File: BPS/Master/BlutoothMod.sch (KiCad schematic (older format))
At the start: 12 parts, among them J12 Conn_01x02, Q5 BSB008NE2LX, U6 RN4870-V_RM118, U7 MCP100-315D

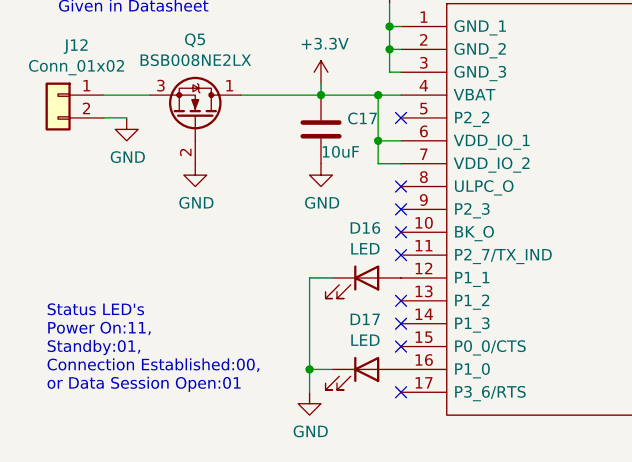
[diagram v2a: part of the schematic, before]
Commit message: Added UART_TX indicator light.
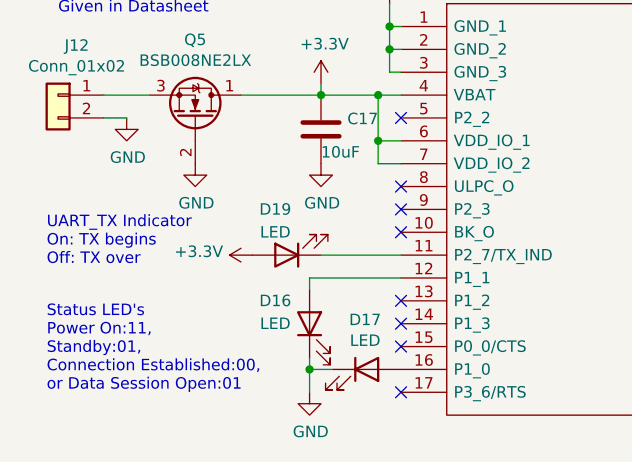
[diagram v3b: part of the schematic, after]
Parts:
- added D19: LED, symbol Device:LED
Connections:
- net +3V3: now also D19.2 (A)
- net at U6.11 (P2_7/TX_IND): now also D19.1 (K)
- no-connect marks 15 -> 14
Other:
- note added: "UART_TX Indicator\nOn: TX begins\nOff: TX over"
- moved on the sheet: D16
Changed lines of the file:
@@
 NoConn ~ 5000 4200
 NoConn ~ 5000 4100
-NoConn ~ 5000 3900
 NoConn ~ 5000 3800
 NoConn ~ 5000 3700
@@
 L Device:LED D16
 U 1 1 5EE20E59
-P 4850 4000
-F 0 "D16" H 4843 4217 50  0000 C CNN
-F 1 "LED" H 4843 4126 50  0000 C CNN
-F 2 "" H 4850 4000 50  0001 C CNN
-F 3 "~" H 4850 4000 50  0001 C CNN
-	1    4850 4000
-	1    0    0    -1
+P 4600 4200
+F 0 "D16" V 4700 4350 50  0000 C CNN
+F 1 "LED" V 4600 4350 50  0000 C CNN
+F 2 "" H 4600 4200 50  0001 C CNN
+F 3 "~" H 4600 4200 50  0001 C CNN
+	1    4600 4200
+	0    -1   -1   0
 $EndComp
 $Comp
@@
 $EndComp
 Wire Wire Line
-	4700 4000 4600 4000
-Wire Wire Line
-	4600 4000 4600 4400
-Wire Wire Line
 	4600 4400 4700 4400
 Wire Wire Line
 	4600 4400 4600 4500
-Connection ~ 4600 4400
 $Comp
 L power:GND #PWR0117
@@
 Text Notes 7450 3600 0    50   ~ 0
 RSSI Indicator\n(On: Strong)
+Wire Wire Line
+	4600 4400 4600 4350
+Connection ~ 4600 4400
+Wire Wire Line
+	4600 4050 4600 4000
+Wire Wire Line
+	4600 4000 5000 4000
+$Comp
+L Device:LED D19
+U 1 1 5EE52339
+P 4500 3900
+F 0 "D19" H 4550 3700 50  0000 C CNN
+F 1 "LED" H 4550 3800 50  0000 C CNN
+F 2 "" H 4500 3900 50  0001 C CNN
+F 3 "~" H 4500 3900 50  0001 C CNN
+	1    4500 3900
+	-1   0    0    1
+$EndComp
+$Comp
+L power:+3.3V #PWR028
+U 1 1 5EE5298C
+P 4350 3900
+F 0 "#PWR028" H 4350 3750 50  0001 C CNN
+F 1 "+3.3V" V 4365 4028 50  0000 L CNN
+F 2 "" H 4350 3900 50  0001 C CNN
+F 3 "" H 4350 3900 50  0001 C CNN
+	1    4350 3900
+	0    -1   -1   0
+$EndComp
+Wire Wire Line
+	4650 3900 5000 3900
+Text Notes 3450 3950 0    50   ~ 0
+UART_TX Indicator\nOn: TX begins\nOff: TX over
 $EndSCHEMATC

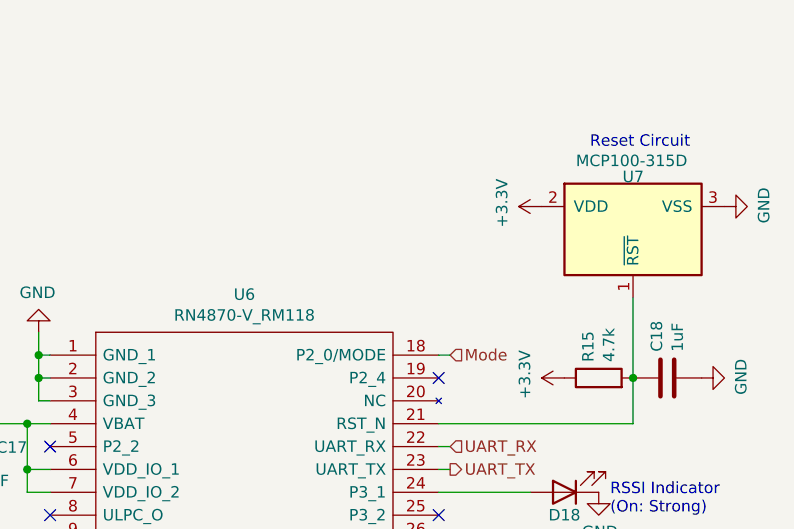
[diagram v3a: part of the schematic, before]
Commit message: The setup for bluetooth mode can't be done through a port using the STM so I used a switch instead, we can use that to toggle between Application mode and testing mode.
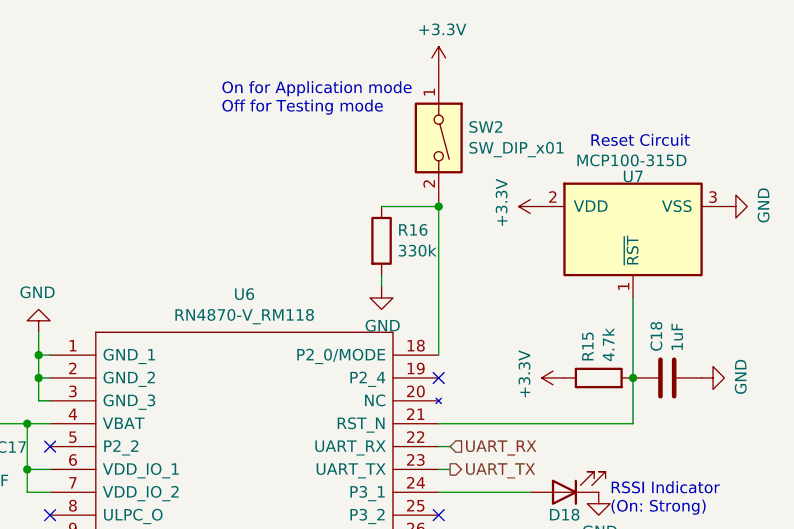
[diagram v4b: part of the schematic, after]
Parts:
- added R16: 330k, symbol Device:R
- added SW2: SW_DIP_x01, symbol Switch:SW_DIP_x01
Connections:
- net +3V3: now also SW2.1
- net GND: now also R16.2
- net Mode: no longer names the net of U6.18 (P2_0/MODE)
- net Mode: now also R16.1, SW2.2
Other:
- note added: "On for Application mode\nOff for Testing mode"
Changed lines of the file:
@@
 	1    0    0    -1
 $EndComp
-Text HLabel 6750 2900 2    50   Input ~ 0
-Mode
 Text Notes 3500 2850 0    50   ~ 0
 Reverse Voltage Protection Circuit\nGiven in Datasheet
@@
 Wire Wire Line
 	6700 3400 6750 3400
-Wire Wire Line
-	6700 2900 6750 2900
 $Comp
 L Power_Supervisor:MCP100-315D U7
@@
 Text Notes 3450 3950 0    50   ~ 0
 UART_TX Indicator\nOn: TX begins\nOff: TX over
+$Comp
+L Switch:SW_DIP_x01 SW2
+U 1 1 5EE36BE3
+P 6700 1950
+F 0 "SW2" V 6654 2080 50  0000 L CNN
+F 1 "SW_DIP_x01" V 6745 2080 50  0000 L CNN
+F 2 "" H 6700 1950 50  0001 C CNN
+F 3 "~" H 6700 1950 50  0001 C CNN
+	1    6700 1950
+	0    1    1    0
+$EndComp
+$Comp
+L power:+3.3V #PWR035
+U 1 1 5EE37A78
+P 6700 1650
+F 0 "#PWR035" H 6700 1500 50  0001 C CNN
+F 1 "+3.3V" H 6715 1823 50  0000 C CNN
+F 2 "" H 6700 1650 50  0001 C CNN
+F 3 "" H 6700 1650 50  0001 C CNN
+	1    6700 1650
+	1    0    0    -1
+$EndComp
+$Comp
+L power:GND #PWR034
+U 1 1 5EE37E2D
+P 6450 2600
+F 0 "#PWR034" H 6450 2350 50  0001 C CNN
+F 1 "GND" H 6455 2427 50  0000 C CNN
+F 2 "" H 6450 2600 50  0001 C CNN
+F 3 "" H 6450 2600 50  0001 C CNN
+	1    6450 2600
+	1    0    0    -1
+$EndComp
+$Comp
+L Device:R R16
+U 1 1 5EE38412
+P 6450 2400
+F 0 "R16" H 6520 2446 50  0000 L CNN
+F 1 "330k" H 6520 2355 50  0000 L CNN
+F 2 "" V 6380 2400 50  0001 C CNN
+F 3 "~" H 6450 2400 50  0001 C CNN
+	1    6450 2400
+	1    0    0    -1
+$EndComp
+Wire Wire Line
+	6450 2550 6450 2600
+Wire Wire Line
+	6450 2250 6700 2250
+Wire Wire Line
+	6700 2250 6700 2900
+Connection ~ 6700 2250
+Text Notes 5750 1850 0    50   ~ 0
+On for Application mode\nOff for Testing mode
 $EndSCHEMATC

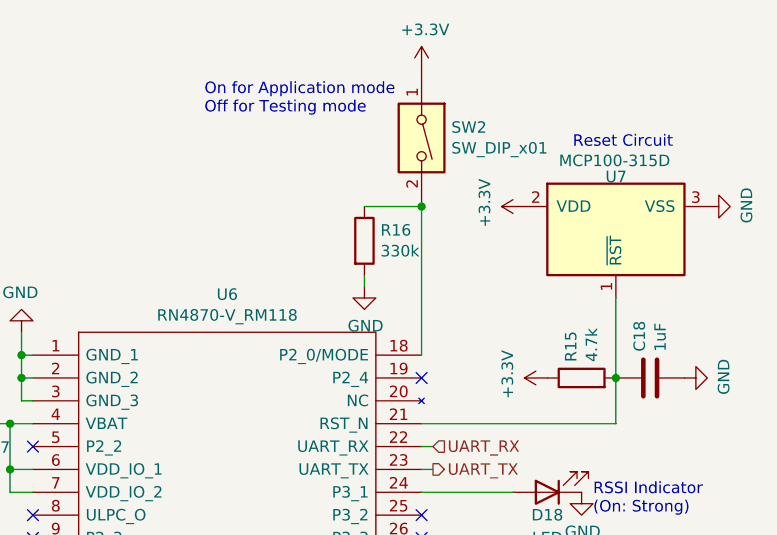
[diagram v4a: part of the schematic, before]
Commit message: Changed resistor values
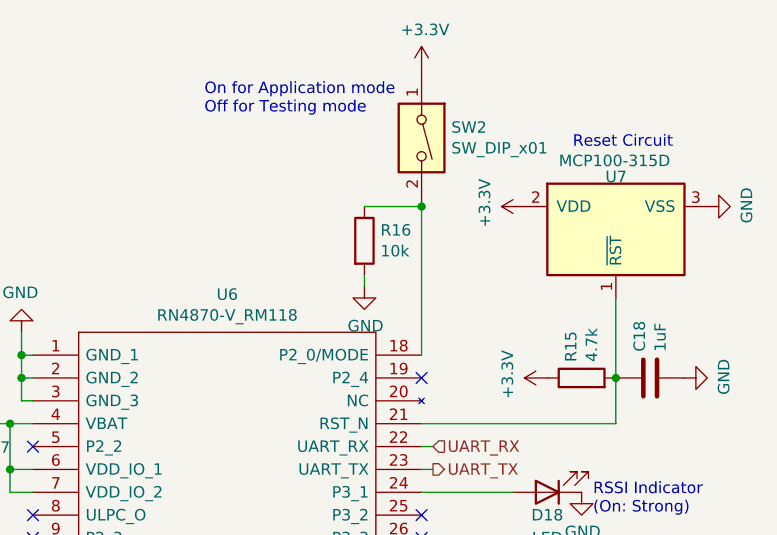
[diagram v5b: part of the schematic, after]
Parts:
- R16: value 330k -> 10k
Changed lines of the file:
@@
 P 6450 2400
 F 0 "R16" H 6520 2446 50  0000 L CNN
-F 1 "330k" H 6520 2355 50  0000 L CNN
+F 1 "10k" H 6520 2355 50  0000 L CNN
 F 2 "" V 6380 2400 50  0001 C CNN
 F 3 "~" H 6450 2400 50  0001 C CNN

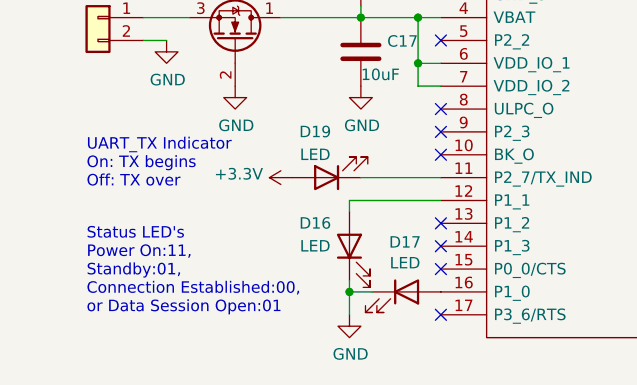
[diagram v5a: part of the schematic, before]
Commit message: Added CTS and RTS connections because we will be sending lots of bytes at a time with the module
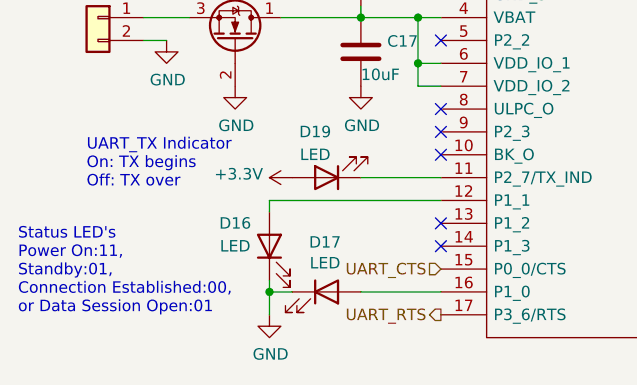
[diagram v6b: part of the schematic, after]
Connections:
- net UART_CTS: now reaches U6.15 (P0_0/CTS)
- net UART_RTS: now reaches U6.17 (P3_6/RTS)
- no-connect marks 14 -> 12
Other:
- moved on the sheet: D16, D17
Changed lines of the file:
@@
 NoConn ~ 6700 3900
 NoConn ~ 6700 4000
-NoConn ~ 5000 4500
-NoConn ~ 5000 4300
 NoConn ~ 5000 4200
 NoConn ~ 5000 4100
@@
 L Device:LED D16
 U 1 1 5EE20E59
-P 4600 4200
-F 0 "D16" V 4700 4350 50  0000 C CNN
-F 1 "LED" V 4600 4350 50  0000 C CNN
-F 2 "" H 4600 4200 50  0001 C CNN
-F 3 "~" H 4600 4200 50  0001 C CNN
-	1    4600 4200
+P 4250 4200
+F 0 "D16" V 4350 4350 50  0000 C CNN
+F 1 "LED" V 4250 4350 50  0000 C CNN
+F 2 "" H 4250 4200 50  0001 C CNN
+F 3 "~" H 4250 4200 50  0001 C CNN
+	1    4250 4200
 	0    -1   -1   0
 $EndComp
@@
 L Device:LED D17
 U 1 1 5EE21939
-P 4850 4400
-F 0 "D17" H 4843 4617 50  0000 C CNN
-F 1 "LED" H 4843 4526 50  0000 C CNN
-F 2 "" H 4850 4400 50  0001 C CNN
-F 3 "~" H 4850 4400 50  0001 C CNN
-	1    4850 4400
+P 4500 4400
+F 0 "D17" H 4493 4617 50  0000 C CNN
+F 1 "LED" H 4493 4526 50  0000 C CNN
+F 2 "" H 4500 4400 50  0001 C CNN
+F 3 "~" H 4500 4400 50  0001 C CNN
+	1    4500 4400
 	1    0    0    -1
 $EndComp
-Wire Wire Line
-	4600 4400 4700 4400
-Wire Wire Line
-	4600 4400 4600 4500
 $Comp
 L power:GND #PWR0117
 U 1 1 5EE2468E
-P 4600 4500
-F 0 "#PWR0117" H 4600 4250 50  0001 C CNN
-F 1 "GND" H 4605 4327 50  0000 C CNN
-F 2 "" H 4600 4500 50  0001 C CNN
-F 3 "" H 4600 4500 50  0001 C CNN
-	1    4600 4500
+P 4250 4500
+F 0 "#PWR0117" H 4250 4250 50  0001 C CNN
+F 1 "GND" H 4255 4327 50  0000 C CNN
+F 2 "" H 4250 4500 50  0001 C CNN
+F 3 "" H 4250 4500 50  0001 C CNN
+	1    4250 4500
 	1    0    0    -1
 $EndComp
 Text Notes 3500 2850 0    50   ~ 0
 Reverse Voltage Protection Circuit\nGiven in Datasheet
-Text Notes 3450 4500 0    50   ~ 0
+Text Notes 3150 4500 0    50   ~ 0
 Status LED's\nPower On:11,\nStandby:01,\nConnection Established:00,\nor Data Session Open:01
 Text Notes 7600 4100 0    50   ~ 0
@@
 Text Notes 7450 3600 0    50   ~ 0
 RSSI Indicator\n(On: Strong)
-Wire Wire Line
-	4600 4400 4600 4350
-Connection ~ 4600 4400
-Wire Wire Line
-	4600 4050 4600 4000
-Wire Wire Line
-	4600 4000 5000 4000
 $Comp
 L Device:LED D19
@@
 Text Notes 5750 1850 0    50   ~ 0
 On for Application mode\nOff for Testing mode
+Wire Wire Line
+	4250 4000 4250 4050
+Wire Wire Line
+	4250 4000 5000 4000
+Wire Wire Line
+	4350 4400 4250 4400
+Wire Wire Line
+	4250 4350 4250 4400
+Connection ~ 4250 4400
+Wire Wire Line
+	4250 4400 4250 4500
+Wire Wire Line
+	4650 4400 5000 4400
+Text HLabel 5000 4300 0    50   Input ~ 0
+UART_CTS
+Text HLabel 5000 4500 0    50   Output ~ 0
+UART_RTS
 $EndSCHEMATC

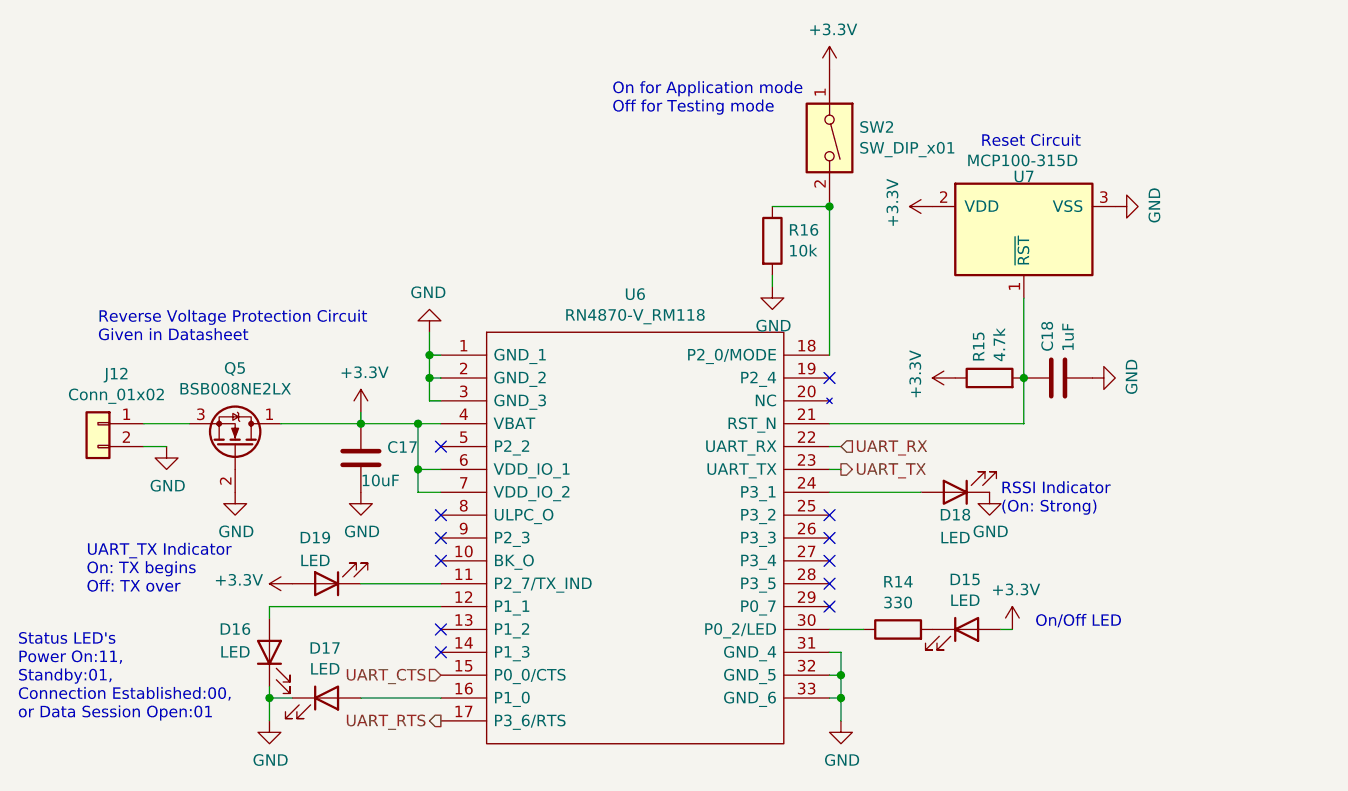
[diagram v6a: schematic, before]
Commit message: Removed the reverse voltage protection circuit because we are not powering it with an external source
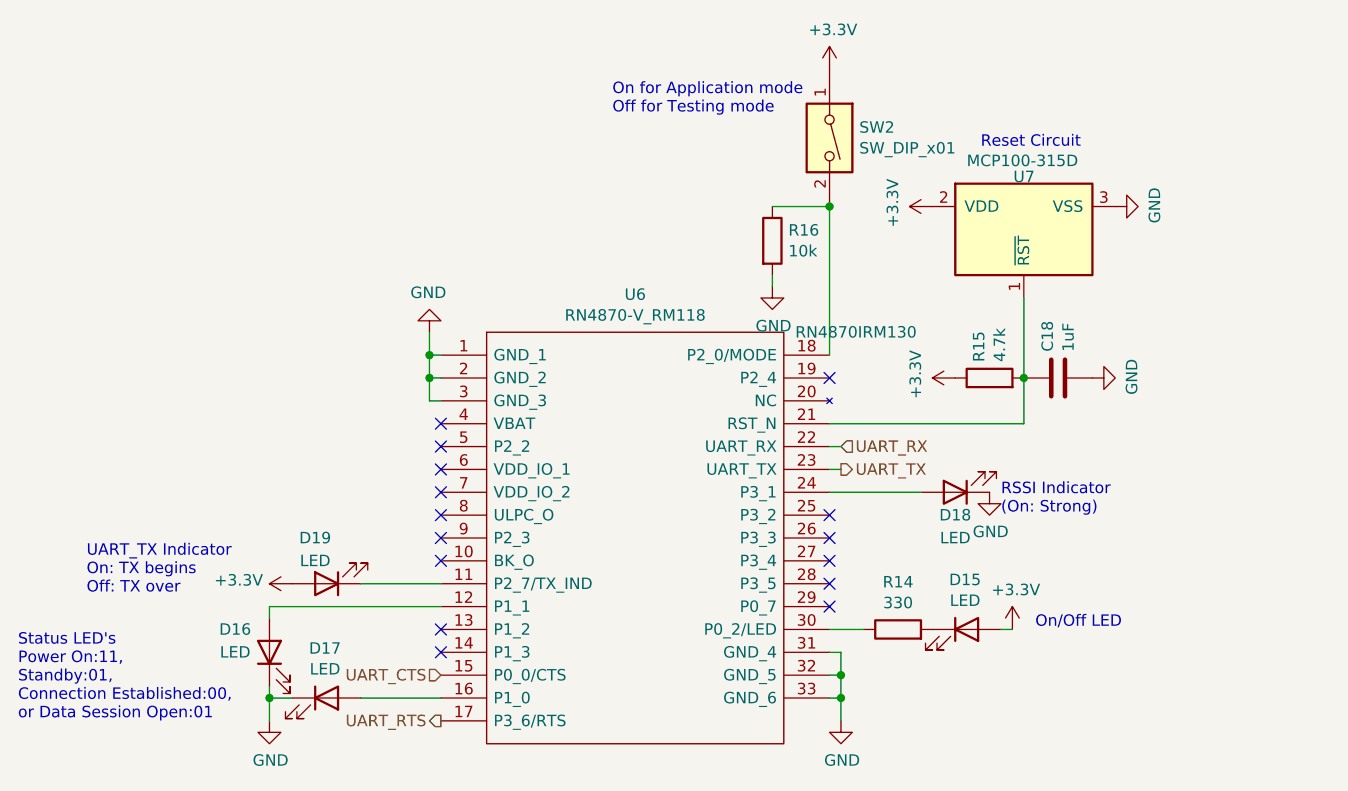
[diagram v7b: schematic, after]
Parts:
- removed C17: 10uF, symbol Device:C
- removed J12: Conn_01x02, symbol Connector_Generic:Conn_01x02
- removed Q5: BSB008NE2LX, Package_DirectFET:DirectFET_MX, symbol Transistor_FET:BSB008NE2LX
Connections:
- net +3V3: no longer U6.4 (VBAT), U6.6 (VDD_IO_1), U6.7 (VDD_IO_2)
- no-connect marks 12 -> 15
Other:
- note removed: "Reverse Voltage Protection Circuit\nGiven in Datasheet"
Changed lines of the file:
@@
 F 0 "U6" H 5850 3165 50  0000 C CNN
 F 1 "RN4870-V_RM118" H 5850 3074 50  0000 C CNN
-F 2 "RN4870IRM130" H 6550 3000 50  0001 L CNN
+F 2 "RN4870IRM130" H 6550 3000 50  0000 L CNN
 F 3 "http://docs-emea.rs-online.com/webdocs/152f/0900766b8152ff8f.pdf" H 6550 2900 50  0001 L CNN
 F 4 "Microchip RN4870-V/RM118 Bluetooth Chip 4.2" H 6550 2800 50  0001 L CNN "Description"
@@
 	1    4950 2800
 	-1   0    0    1
-$EndComp
-Wire Wire Line
-	5000 3200 4900 3200
-Wire Wire Line
-	4900 3200 4900 3400
-Wire Wire Line
-	4900 3400 5000 3400
-Wire Wire Line
-	4900 3400 4900 3500
-Wire Wire Line
-	4900 3500 5000 3500
-Connection ~ 4900 3400
-Connection ~ 4900 3200
-$Comp
-L power:GND #PWR0108
-U 1 1 5EE4ABF0
-P 4650 3500
-F 0 "#PWR0108" H 4650 3250 50  0001 C CNN
-F 1 "GND" H 4655 3327 50  0000 C CNN
-F 2 "" H 4650 3500 50  0001 C CNN
-F 3 "" H 4650 3500 50  0001 C CNN
-	1    4650 3500
-	1    0    0    -1
-$EndComp
-$Comp
-L power:+3.3V #PWR0109
-U 1 1 5EE4AD11
-P 4650 3150
-F 0 "#PWR0109" H 4650 3000 50  0001 C CNN
-F 1 "+3.3V" H 4665 3323 50  0000 C CNN
-F 2 "" H 4650 3150 50  0001 C CNN
-F 3 "" H 4650 3150 50  0001 C CNN
-	1    4650 3150
-	1    0    0    -1
-$EndComp
-$Comp
-L Device:C C17
-U 1 1 5EE4B59B
-P 4650 3350
-F 0 "C17" H 4765 3396 50  0000 L CNN
-F 1 "10uF" H 4650 3250 50  0000 L CNN
-F 2 "" H 4688 3200 50  0001 C CNN
-F 3 "~" H 4650 3350 50  0001 C CNN
-	1    4650 3350
-	1    0    0    -1
-$EndComp
-Connection ~ 4650 3200
-Wire Wire Line
-	4650 3200 4900 3200
-Wire Wire Line
-	4650 3200 4650 3150
-Wire Wire Line
-	4650 3200 4300 3200
-$Comp
-L Transistor_FET:BSB008NE2LX Q5
-U 1 1 5EE62400
-P 4100 3300
-F 0 "Q5" V 4442 3300 50  0000 C CNN
-F 1 "BSB008NE2LX" V 4351 3300 50  0000 C CNN
-F 2 "Package_DirectFET:DirectFET_MX" H 4100 3300 50  0001 C CIN
-F 3 "https://www.infineon.com/dgdl/Infineon-BSB008NE2LX-DS-v02_00-EN.pdf?fileId=db3a30432e564707012e5745ca7d000e" H 4100 3300 50  0001 L CNN
-	1    4100 3300
-	0    1    -1   0
-$EndComp
-$Comp
-L power:GND #PWR0110
-U 1 1 5EE6457A
-P 4100 3500
-F 0 "#PWR0110" H 4100 3250 50  0001 C CNN
-F 1 "GND" H 4105 3327 50  0000 C CNN
-F 2 "" H 4100 3500 50  0001 C CNN
-F 3 "" H 4100 3500 50  0001 C CNN
-	1    4100 3500
-	1    0    0    -1
-$EndComp
-$Comp
-L Connector_Generic:Conn_01x02 J12
-U 1 1 5EE69056
-P 3500 3200
-F 0 "J12" H 3418 3417 50  0000 C CNN
-F 1 "Conn_01x02" H 3418 3326 50  0000 C CNN
-F 2 "" H 3500 3200 50  0001 C CNN
-F 3 "~" H 3500 3200 50  0001 C CNN
-	1    3500 3200
-	-1   0    0    -1
-$EndComp
-Wire Wire Line
-	3700 3200 3900 3200
-Wire Wire Line
-	3700 3300 3800 3300
-$Comp
-L power:GND #PWR0111
-U 1 1 5EE6AECF
-P 3800 3300
-F 0 "#PWR0111" H 3800 3050 50  0001 C CNN
-F 1 "GND" H 3805 3127 50  0000 C CNN
-F 2 "" H 3800 3300 50  0001 C CNN
-F 3 "" H 3800 3300 50  0001 C CNN
-	1    3800 3300
-	1    0    0    -1
 $EndComp
 $Comp
@@
 	1    0    0    -1
 $EndComp
-Text Notes 3500 2850 0    50   ~ 0
-Reverse Voltage Protection Circuit\nGiven in Datasheet
 Text Notes 3150 4500 0    50   ~ 0
 Status LED's\nPower On:11,\nStandby:01,\nConnection Established:00,\nor Data Session Open:01
@@
 Text HLabel 5000 4500 0    50   Output ~ 0
 UART_RTS
+NoConn ~ 5000 3500
+NoConn ~ 5000 3400
+NoConn ~ 5000 3200
 $EndSCHEMATC
